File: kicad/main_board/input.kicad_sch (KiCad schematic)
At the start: 38 parts, among them J1 USB_C, J2 TRIG_A, J3 TRIG_B, Q1 DMP3018SFV, Q2 DMN63D8LW, U1 SRV05-4, U2 SRV05-4, U3 FUSB302B

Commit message: add audio
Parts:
- removed TP3: VRAW, TestPoint:TestPoint_Pad_D1.0mm, symbol Connector:TestPoint_Small
- renumbered TP4 to TP3, TP5 to TP4, TP6 to TP5
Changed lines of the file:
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@@
 	)
 	(junction
-		(at 43.18 27.94)
-		(diameter 0)
-		(color 0 0 0 0)
-	)
-	(junction
 		(at 156.21 41.91)
 		(diameter 0)
@@
 	(wire
 		(pts
-			(xy 41.91 27.94) (xy 43.18 27.94)
-		)
-		(stroke
-			(width 0)
-			(type default)
-		)
-	)
-	(wire
-		(pts
 			(xy 36.83 135.89) (xy 49.53 135.89)
 		)
@@
 	(wire
 		(pts
-			(xy 43.18 25.4) (xy 43.18 27.94)
-		)
-		(stroke
-			(width 0)
-			(type default)
-		)
-	)
-	(wire
-		(pts
 			(xy 40.64 129.54) (xy 40.64 133.35)
 		)
@@
 	(wire
 		(pts
-			(xy 43.18 27.94) (xy 76.2 27.94)
+			(xy 41.91 27.94) (xy 76.2 27.94)
 		)
 		(stroke
@@
 	(text "20V @ 5A"
 		(exclude_from_sim no)
-		(at 52.578 24.13 0)
+		(at 50.292 26.162 0)
 		(effects
 			(font
@@
 		(dnp no)
 		(fields_autoplaced yes)
-		(property "Reference" "TP5"
+		(property "Reference" "TP4"
 			(at 40.64 60.706 0)
 			(effects
@@
 			(project "main_board"
 				(path "/8e1f1504-76c2-49e6-9261-3c1190503f8c/0962b75e-3e22-438c-afab-e79e573b4781"
-					(reference "TP5")
+					(reference "TP4")
 					(unit 1)
 				)
@@
 		(on_board yes)
 		(dnp no)
-		(fields_autoplaced yes)
-		(property "Reference" "TP4"
+		(property "Reference" "TP3"
 			(at 44.45 54.6099 0)
 			(effects
@@
 			(project "main_board"
 				(path "/8e1f1504-76c2-49e6-9261-3c1190503f8c/0962b75e-3e22-438c-afab-e79e573b4781"
-					(reference "TP4")
+					(reference "TP3")
 					(unit 1)
 				)
@@
 		(on_board yes)
 		(dnp no)
-		(property "Reference" "TP6"
+		(property "Reference" "TP5"
 			(at 76.2 21.082 0)
 			(effects
@@
 			(project "main_board"
 				(path "/8e1f1504-76c2-49e6-9261-3c1190503f8c/0962b75e-3e22-438c-afab-e79e573b4781"
-					(reference "TP6")
+					(reference "TP5")
 					(unit 1)
 				)
@@
 					(unit 1)
 				)
-			)
-		)
-	)
-	(symbol
-		(lib_id "Connector:TestPoint_Small")
-		(at 43.18 25.4 0)
-		(mirror y)
-		(unit 1)
-		(exclude_from_sim no)
-		(in_bom no)
-		(on_board yes)
-		(dnp no)
-		(property "Reference" "TP3"
-			(at 43.18 21.082 0)
-			(effects
-				(font
-					(size 1.27 1.27)
-				)
-			)
-		)
-		(property "Value" "VRAW"
-			(at 43.18 23.622 0)
-			(effects
-				(font
-					(size 1.27 1.27)
-				)
-			)
-		)
-		(property "Footprint" "TestPoint:TestPoint_Pad_D1.0mm"
-			(at 38.1 25.4 0)
-			(effects
-				(font
-					(size 1.27 1.27)
-				)
-				(hide yes)
-			)
-		)
-		(property "Datasheet" "~"
-			(at 38.1 25.4 0)
-			(effects
-				(font
-					(size 1.27 1.27)
-				)
-				(hide yes)
-			)
-		)
-		(property "Description" "test point"
-			(at 43.18 25.4 0)
-			(effects
-				(font
-					(size 1.27 1.27)
-				)
-				(hide yes)
-			)
-		)
-		(property "MPN" ""
-			(at 43.18 25.4 0)
-			(effects
-				(font
-					(size 1.27 1.27)
-				)
-				(hide yes)
-			)
-		)
-		(property "MPN_ALT" ""
-			(at 43.18 25.4 0)
-			(effects
-				(font
-					(size 1.27 1.27)
-				)
-				(hide yes)
-			)
-		)
-		(property "LCSC" ""
-			(at 43.18 25.4 0)
-			(effects
-				(font
-					(size 1.27 1.27)
-				)
-				(hide yes)
-			)
-		)
-		(property "MOUSER" ""
-			(at 43.18 25.4 0)
-			(effects
-				(font
-					(size 1.27 1.27)
-				)
-				(hide yes)
-			)
-		)
-		(pin "1"
-		)
-		(instances
-			(project "main_board"
-				(path "/8e1f1504-76c2-49e6-9261-3c1190503f8c/0962b75e-3e22-438c-afab-e79e573b4781"
-					(reference "TP3")
-					(unit 1)
-				)

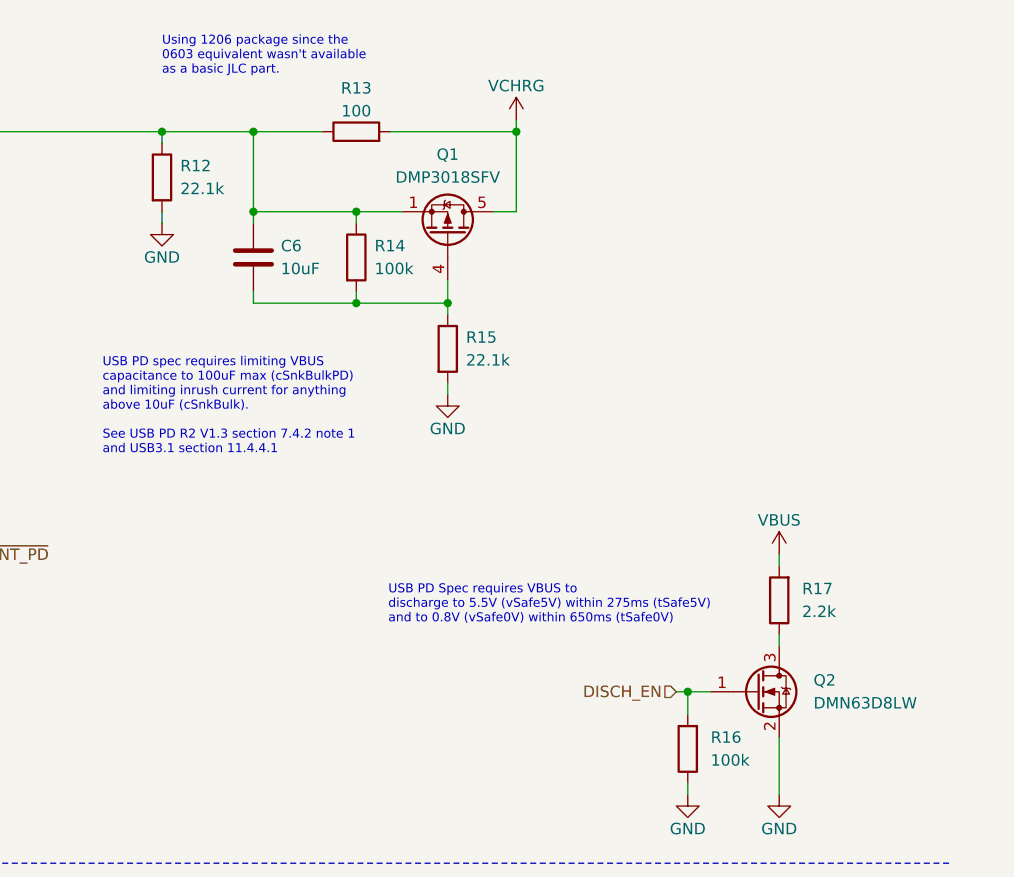
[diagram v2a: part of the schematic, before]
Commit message: update BOM prioritizing basic parts
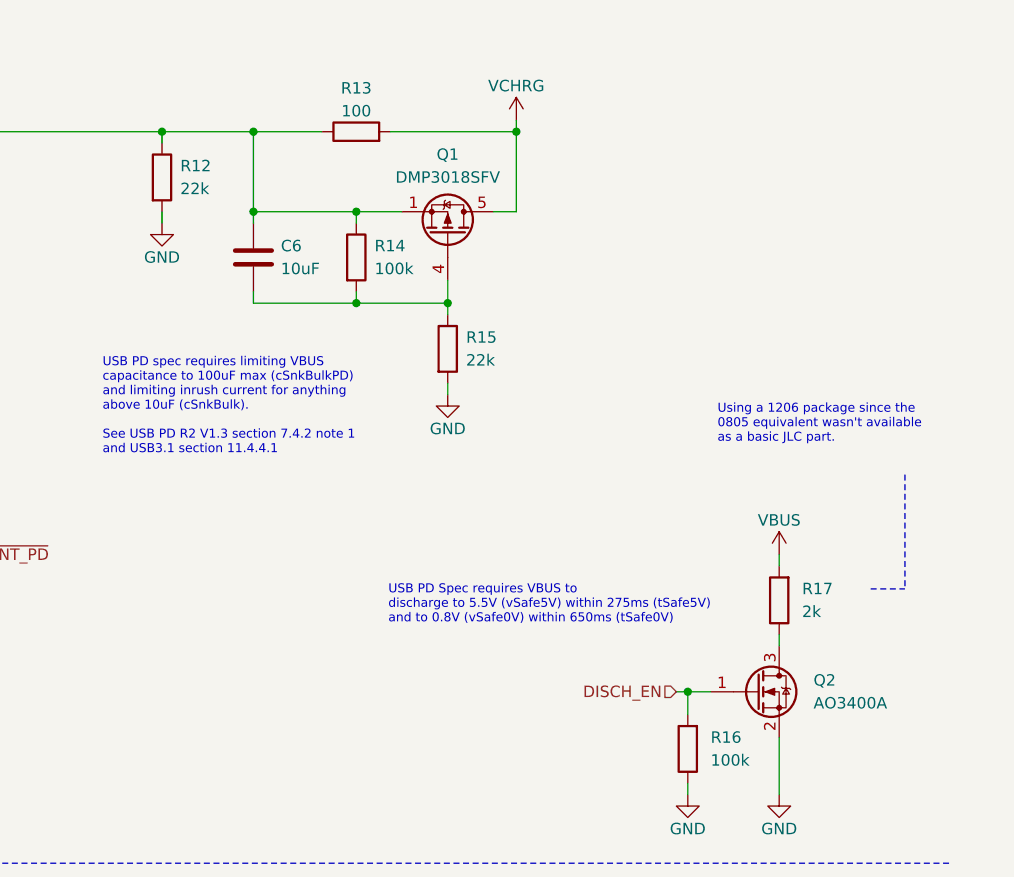
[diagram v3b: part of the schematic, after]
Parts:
- C1, C2: JLC (none) -> C1664; LCSC C307487 -> (none); MOUSER 187-CL10B331KB8NNNC -> (none); MPN CL10B331KB8NNNC -> (none)
- C3, C6: JLC (none) -> C96446; LCSC C96446 -> (none); MOUSER 187-CL10A106MA8NRNC -> (none); MPN CL10A106MA8NRNC -> (none)
- C4: JLC (none) -> C15849; LCSC C5199872 -> (none); MOUSER 187-CL10B105KB8NQNC -> (none); MPN CL10B105KB8NQNC -> (none)
- C5: JLC (none) -> C14663; LCSC C1591 -> (none); MOUSER 187-CL10B104KB8NNNC -> (none); MPN CL10B104KB8NNNC -> (none)
- D1: footprint Diode_SMD:ST_QFN-2L_1.6x1.0mm -> (none); LCSC C1974707 -> (none); MOUSER 511-ESDA25P35-1U1M -> (none); MPN ESDA25P35-1U1M -> (none)
- J1: JLC (none) -> C2765186; MOUSER 640-USB4105-GF-A -> (none); MPN USB4105-GF-A -> (none)
- J2, J3: footprint SaawLib:STX-3100-5N -> SaawLib:PJ-3062-CO; LCSC (none) -> C319113; MOUSER 806-STX-3100-5N -> (none); MPN STX-3100-5N -> (none)
- Q1: JLC (none) -> C461075; LCSC C461075 -> (none); MOUSER 621-DMP3018SFV-7 -> (none); MPN DMP3018SFV-7 -> (none)
- Q2: value DMN63D8LW -> AO3400A; footprint Package_TO_SOT_SMD:SOT-323_SC-70 -> Package_TO_SOT_SMD:SOT-23; JLC (none) -> C20917; LCSC C151057 -> (none); MOUSER 621-DMN63D8LW-7 -> (none); MPN DMN63D8LW-7 -> (none)
- R1, R11, R2, R3, R4: JLC (none) -> C25804; LCSC C25804 -> (none); MOUSER 603-RC0603FR-0710KL -> (none); MPN RC0603FR-0710KL -> (none)
- R10, R14, R16, R5: JLC (none) -> C25803; LCSC C25803 -> (none); MOUSER 603-RC0603FR-07100KL -> (none); MPN RC0603FR-07100KL -> (none)
- R12, R15: value 22.1k -> 22k; JLC (none) -> C31850; LCSC C25961 -> (none); MOUSER 603-RC0603FR-0722K1L -> (none); MPN RC0603FR-0722K1L -> (none)
- R13: JLC (none) -> C17901; LCSC C17901 -> (none); MOUSER 603-RC1206FR-07100RL -> (none); MPN RC1206FR-07100RL -> (none)
- R17: value 2.2k -> 2k; footprint Resistor_SMD:R_0603_1608Metric -> Resistor_SMD:R_1206_3216Metric; JLC (none) -> C17944; LCSC C7336403 -> (none); MOUSER 603-RC0603FR-7W2K2L -> (none); MPN RC0603FR-7W2K2L -> (none)
- R6, R7, R8, R9: JLC (none) -> C21190; LCSC C21190 -> (none); MOUSER 603-RC0603FR-071KL -> (none); MPN RC0603FR-071KL -> (none)
- U1, U2: JLC (none) -> C111212; LCSC C111212 -> (none); MOUSER 511-USBLC6-4SC6 -> (none); MPN USBLC6-4SC6 -> (none); MPN_ALT SRV05-4L-TP -> (none)
- U3: JLC (none) -> C132291; LCSC C132291 -> (none); MOUSER 512-FUSB302BMPX -> (none); MPN FUSB302BMPX -> (none)
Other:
- note added: "Using a 1206 package since the 0805 equivalent wasn't available as a basic JLC part."
- note removed: "Using 1206 package since the 0603 equivalent wasn't available as a basic JLC part."

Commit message: add generation script
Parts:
- C1, C2: JLC C1664 -> (none); LCSC (none) -> C1664; Service (none) -> PCBA
- C3, C6: JLC C96446 -> (none); LCSC (none) -> C96446; Service (none) -> PCBA
- C4: JLC C15849 -> (none); LCSC (none) -> C15849; Service (none) -> PCBA
- C5: JLC C14663 -> (none); LCSC (none) -> C14663; Service (none) -> PCBA
- D1: Service (none) -> PCBA
- J1: JLC C2765186 -> (none); LCSC (none) -> C2765186; Service (none) -> PCBA
- J2, J3: Service (none) -> HandAssembly
- Q1: JLC C461075 -> (none); LCSC (none) -> C461075; Service (none) -> PCBA
- Q2: JLC C20917 -> (none); LCSC (none) -> C20917; Service (none) -> PCBA
- R1, R11, R2, R3, R4: JLC C25804 -> (none); LCSC (none) -> C25804; Service (none) -> PCBA
- R10, R14, R16, R5: JLC C25803 -> (none); LCSC (none) -> C25803; Service (none) -> PCBA
- R12, R15: JLC C31850 -> (none); LCSC (none) -> C31850; Service (none) -> PCBA
- R13: JLC C17901 -> (none); LCSC (none) -> C17901; Service (none) -> PCBA
- R17: JLC C17944 -> (none); LCSC (none) -> C17944; Service (none) -> PCBA
- R6, R7, R8, R9: JLC C21190 -> (none); LCSC (none) -> C21190; Service (none) -> PCBA
- TP1, TP2, TP3, TP4, TP5: Service (none) -> PCBA;HandAssembly
- U1, U2: JLC C111212 -> (none); LCSC (none) -> C111212; Service (none) -> PCBA
- U3: JLC C132291 -> (none); LCSC (none) -> C132291; Service (none) -> PCBA
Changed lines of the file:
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@@
 			)
 		)
-		(property "JLC" ""
+		(property "Service" "PCBA;HandAssembly"
 			(at 43.18 58.42 0)
 			(effects
@@
 			)
 		)
-		(property "LCSC" ""
+		(property "LCSC" "C461075"
 			(at 228.6 39.37 0)
 			(effects
@@
 			)
 		)
-		(property "JLC" "C461075"
+		(property "Service" "PCBA"
 			(at 228.6 39.37 0)
 			(effects
@@
 			)
 		)
-		(property "LCSC" ""
+		(property "LCSC" "C21190"
 			(at 76.2 177.8 0)
 			(effects
@@
 			)
 		)
-		(property "JLC" "C21190"
+		(property "Service" "PCBA"
 			(at 76.2 177.8 0)
 			(effects
@@
 			)
 		)
-		(property "JLC" ""
+		(property "Service" "HandAssembly"
 			(at 31.75 177.8 0)
 			(effects
@@
 			)
 		)
-		(property "LCSC" ""
+		(property "LCSC" "C21190"
 			(at 76.2 175.26 0)
 			(effects
@@
 			)
 		)
-		(property "JLC" "C21190"
+		(property "Service" "PCBA"
 			(at 76.2 175.26 0)
 			(effects
@@
 			)
 		)
-		(property "LCSC" ""
+		(property "LCSC" "C1664"
 			(at 85.09 40.64 0)
 			(effects
@@
 			)
 		)
-		(property "JLC" "C1664"
+		(property "Service" "PCBA"
 			(at 85.09 40.64 0)
 			(effects
@@
 			)
 		)
-		(property "LCSC" ""
+		(property "LCSC" "C25804"
 			(at 167.64 69.85 0)
 			(effects
@@
 			)
 		)
-		(property "JLC" "C25804"
+		(property "Service" "PCBA"
 			(at 167.64 69.85 0)
 			(effects
@@
 			)
 		)
-		(property "LCSC" ""
+		(property "LCSC" "C17901"
 			(at 218.44 27.94 0)
 			(effects
@@
 			)
 		)
-		(property "JLC" "C17901"
+		(property "Service" "PCBA"
 			(at 218.44 27.94 0)
 			(effects
@@
 			)
 		)
-		(property "LCSC" ""
+		(property "LCSC" "C25804"
 			(at 40.64 167.64 0)
 			(effects
@@
 			)
 		)
-		(property "JLC" "C25804"
+		(property "Service" "PCBA"
 			(at 40.64 167.64 0)
 			(effects
@@
 			)
 		)
-		(property "LCSC" ""
+		(property "LCSC" "C25804"
 			(at 40.64 125.73 0)
 			(effects
@@
 			)
 		)
-		(property "JLC" "C25804"
+		(property "Service" "PCBA"
 			(at 40.64 125.73 0)
 			(effects
@@
 			)
 		)
-		(property "LCSC" ""
+		(property "LCSC" "C25804"
 			(at 49.53 125.73 0)
 			(effects
@@
 			)
 		)
-		(property "JLC" "C25804"
+		(property "Service" "PCBA"
 			(at 49.53 125.73 0)
 			(effects
@@
 			)
 		)
-		(property "LCSC" ""
+		(property "LCSC" "C20917"
 			(at 262.89 90.17 0)
 			(effects
@@
 			)
 		)
-		(property "JLC" "C20917"
+		(property "Service" "PCBA"
 			(at 262.89 90.17 0)
 			(effects
@@
 			)
 		)
-		(property "LCSC" ""
+		(property "LCSC" "C21190"
 			(at 76.2 135.89 0)
 			(effects
@@
 			)
 		)
-		(property "JLC" "C21190"
+		(property "Service" "PCBA"
 			(at 76.2 135.89 0)
 			(effects
@@
 			)
 		)
-		(property "JLC" ""
+		(property "Service" "PCBA;HandAssembly"
 			(at 34.29 100.33 0)
 			(effects
@@
 			)
 		)
-		(property "LCSC" ""
+		(property "LCSC" "C25803"
 			(at 125.73 139.7 0)
 			(effects
@@
 			)
 		)
-		(property "JLC" "C25803"
+		(property "Service" "PCBA"
 			(at 125.73 139.7 0)
 			(effects
@@
 			)
 		)
-		(property "LCSC" ""
+		(property "LCSC" "C25803"
 			(at 255.27 96.52 0)
 			(effects
@@
 			)
 		)
-		(property "JLC" "C25803"
+		(property "Service" "PCBA"
 			(at 255.27 96.52 0)
 			(effects
@@
 			)
 		)
-		(property "LCSC" ""
+		(property "LCSC" "C17944"
 			(at 265.43 80.01 0)
 			(effects
@@
 			)
 		)
-		(property "JLC" "C17944"
+		(property "Service" "PCBA"
 			(at 265.43 80.01 0)
 			(effects
@@
 			)
 		)
-		(property "LCSC" ""
+		(property "LCSC" "C111212"
 			(at 125.73 157.48 0)
 			(effects
@@
 			)
 		)
-		(property "JLC" "C111212"
+		(property "Service" "PCBA"
 			(at 125.73 157.48 0)
 			(effects
@@
 			)
 		)
-		(property "LCSC" ""
+		(property "LCSC" "C31850"
 			(at 196.85 33.02 0)
 			(effects
@@
 			)
 		)
-		(property "JLC" "C31850"
+		(property "Service" "PCBA"
 			(at 196.85 33.02 0)
 			(effects
@@
 			)
 		)
-		(property "LCSC" ""
+		(property "LCSC" "C15849"
 			(at 144.78 46.99 0)
 			(effects
@@
 			)
 		)
-		(property "JLC" "C15849"
+		(property "Service" "PCBA"
 			(at 144.78 46.99 0)
 			(effects
@@
 			)
 		)
-		(property "JLC" ""
+		(property "Service" "HandAssembly"
 			(at 31.75 135.89 0)
 			(effects
@@
 			)
 		)
-		(property "JLC" ""
+		(property "Service" "PCBA;HandAssembly"
 			(at 40.64 100.33 0)
 			(effects
@@
 			)
 		)
-		(property "LCSC" ""
+		(property "LCSC" "C96446"
 			(at 207.01 41.91 0)
 			(effects
@@
 			)
 		)
-		(property "JLC" "C96446"
+		(property "Service" "PCBA"
 			(at 207.01 41.91 0)
 			(effects
@@
 			)
 		)
-		(property "LCSC" ""
+		(property "LCSC" "C21190"
 			(at 76.2 133.35 0)
 			(effects
@@
 			)
 		)
-		(property "JLC" "C21190"
+		(property "Service" "PCBA"
 			(at 76.2 133.35 0)
 			(effects
@@
 			)
 		)
-		(property "LCSC" ""
+		(property "LCSC" "C25803"
 			(at 218.44 41.91 0)
 			(effects
@@
 			)
 		)
-		(property "JLC" "C25803"
+		(property "Service" "PCBA"
 			(at 218.44 41.91 0)
 			(effects
@@
 			)
 		)
-		(property "LCSC" ""
+		(property "LCSC" "C25804"
 			(at 49.53 167.64 0)
 			(effects
@@
 			)
 		)
-		(property "JLC" "C25804"
+		(property "Service" "PCBA"
 			(at 49.53 167.64 0)
 			(effects
@@
 			)
 		)
-		(property "LCSC" ""
+		(property "LCSC" "C132291"
 			(at 134.62 72.39 0)
 			(effects
@@
 			)
 		)
-		(property "JLC" "C132291"
+		(property "Service" "PCBA"
 			(at 134.62 72.39 0)
 			(effects
@@
 			)
 		)
-		(property "LCSC" ""
+		(property "LCSC" "C111212"
 			(at 74.93 87.63 0)
 			(effects
@@
 			)
 		)
-		(property "JLC" "C111212"
+		(property "Service" "PCBA"
 			(at 74.93 87.63 0)
 			(effects
@@
 			)
 		)
-		(property "LCSC" ""
+		(property "LCSC" "C14663"
 			(at 156.21 46.99 0)
 			(effects
@@
 			)
 		)
-		(property "JLC" "C14663"
+		(property "Service" "PCBA"
 			(at 156.21 46.99 0)
 			(effects
@@
 			)
 		)
-		(property "JLC" ""
+		(property "Service" "PCBA;HandAssembly"
 			(at 43.18 55.88 0)
 			(effects
@@
 			)
 		)
-		(property "LCSC" ""
+		(property "LCSC" "C31850"
 			(at 228.6 52.07 0)
 			(effects
@@
 			)
 		)
-		(property "JLC" "C31850"
+		(property "Service" "PCBA"
 			(at 228.6 52.07 0)
 			(effects
@@
 			)
 		)
-		(property "LCSC" ""
+		(property "LCSC" "C1664"
 			(at 73.66 40.64 0)
 			(effects
@@
 			)
 		)
-		(property "JLC" "C1664"
+		(property "Service" "PCBA"
 			(at 73.66 40.64 0)
 			(effects
@@
 			)
 		)
-		(property "LCSC" ""
+		(property "LCSC" "C2765186"
 			(at 26.67 43.18 0)
 			(effects
@@
 			)
 		)
-		(property "JLC" "C2765186"
+		(property "Service" "PCBA"
 			(at 26.67 43.18 0)
 			(effects
@@
 			)
 		)
-		(property "JLC" ""
+		(property "Service" "PCBA;HandAssembly"
 			(at 76.2 25.4 0)
 			(effects
@@
 			)
 		)
-		(property "JLC" ""
+		(property "Service" "PCBA"
 			(at 21.59 96.52 0)
 			(effects
@@
 			)
 		)
-		(property "LCSC" ""
+		(property "LCSC" "C25803"
 			(at 74.93 69.85 0)
 			(effects
@@
 			)
 		)
-		(property "JLC" "C25803"
+		(property "Service" "PCBA"
 			(at 74.93 69.85 0)
 			(effects
@@
 			)
 		)
-		(property "LCSC" ""
+		(property "LCSC" "C96446"
 			(at 124.46 46.99 0)
 			(effects
@@
 			)
 		)
-		(property "JLC" "C96446"
+		(property "Service" "PCBA"
 			(at 124.46 46.99 0)
 			(effects

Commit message: add VBUS tvs
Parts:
- D1: footprint (none) -> Diode_SMD:ST_QFN-2L_1.6x1.0mm; LCSC (none) -> C1974707
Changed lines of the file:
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@@
 			)
 		)
-		(property "Footprint" ""
+		(property "Footprint" "Diode_SMD:ST_QFN-2L_1.6x1.0mm"
 			(at 21.59 96.52 0)
 			(effects
@@
 			)
 		)
-		(property "Datasheet" "~"
+		(property "Datasheet" "https://www.lcsc.com/datasheet/lcsc_datasheet_2201300300_STMicroelectronics-ESDA25P35-1U1M_C1974707.pdf"
 			(at 21.59 96.52 0)
 			(effects
@@
 			)
 		)
-		(property "LCSC" ""
+		(property "LCSC" "C1974707"
 			(at 21.59 96.52 0)
 			(effects
